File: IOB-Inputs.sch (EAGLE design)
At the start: 22 parts, among them J1 RJ12/6, Q0 P-FET, Q1 P-FET, Q2 P-FET, Q3 P-FET

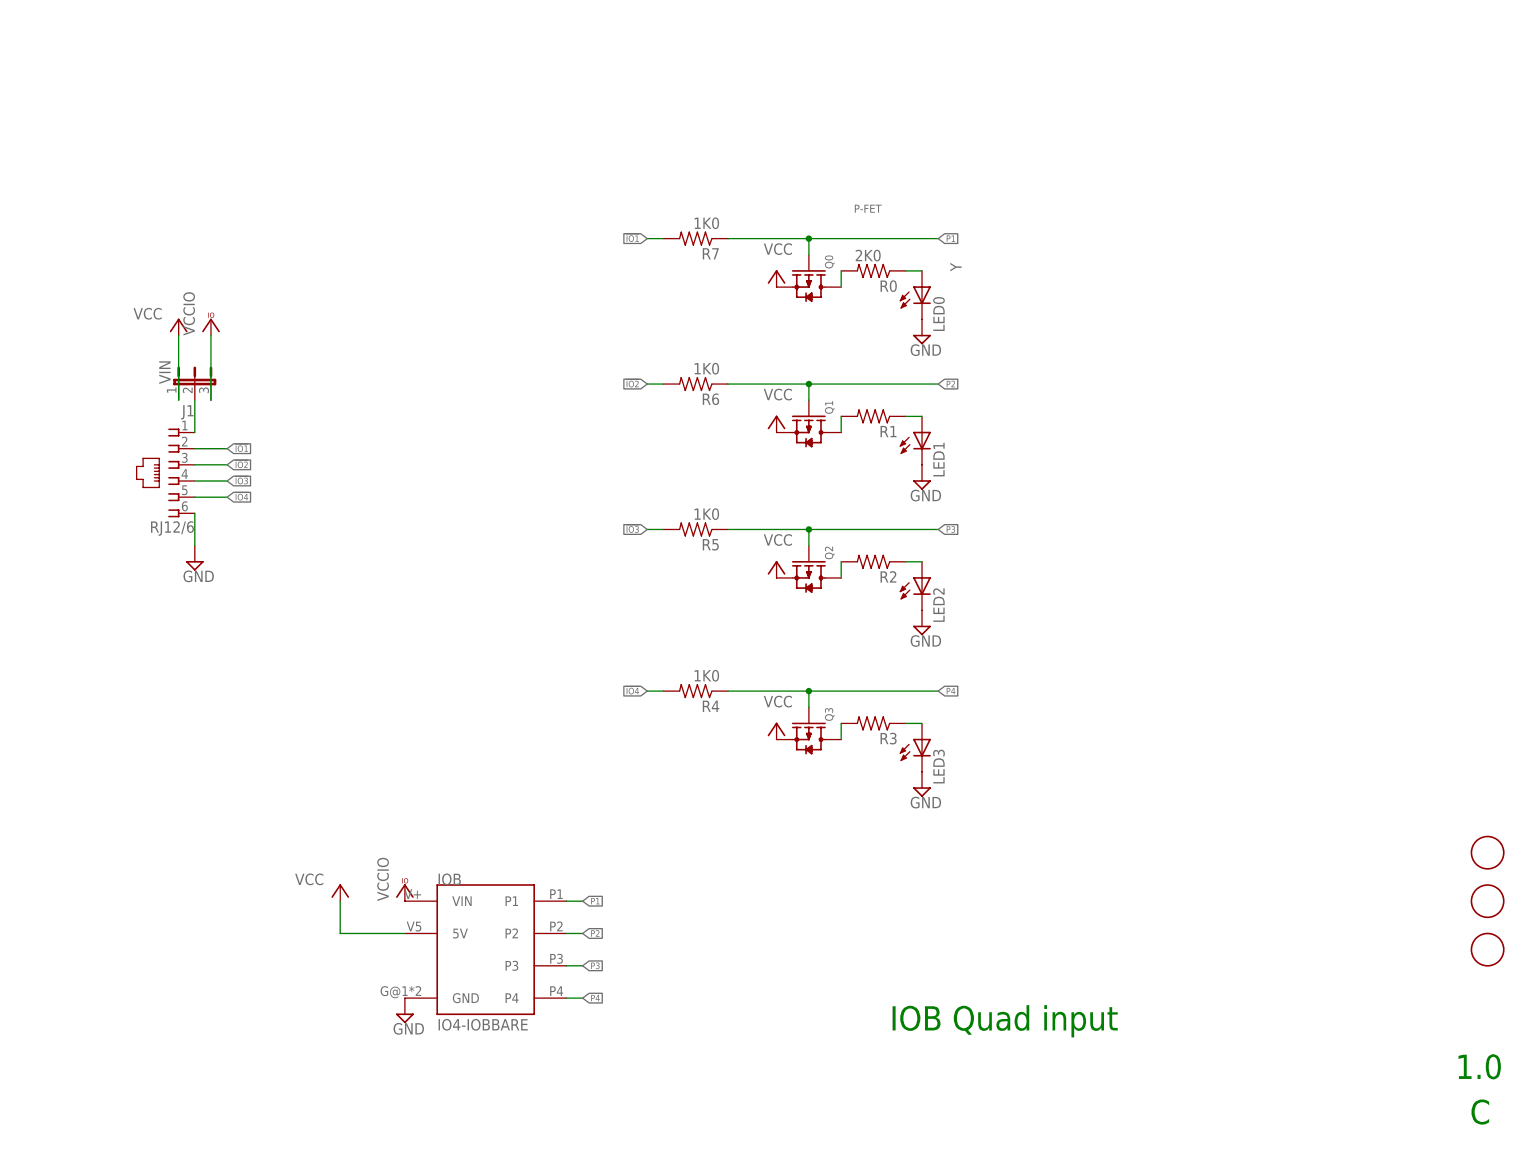
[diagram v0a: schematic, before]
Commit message: added input protection diodes and RC filter to handle 1khz or less signals
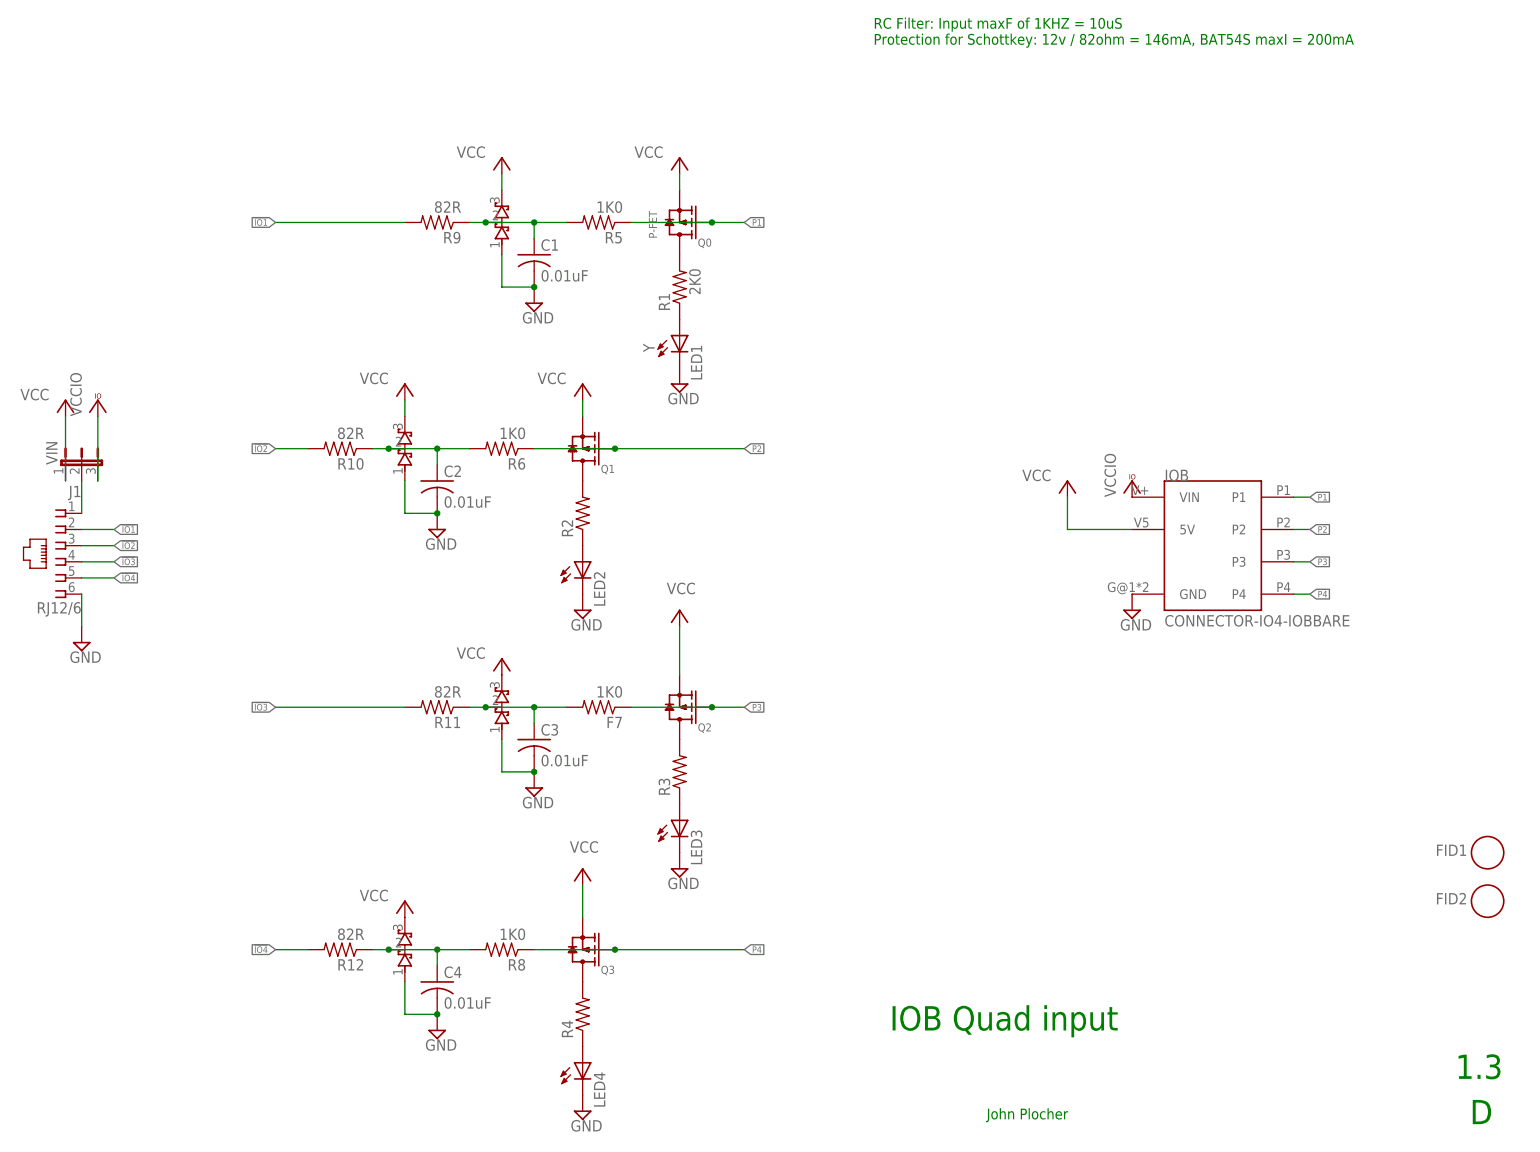
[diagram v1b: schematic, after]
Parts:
- removed FID3: FIDUCIAL, SPCoast:FIDUCIAL
- removed LED0: Y, SPCoast:LED0603-LED
- removed R0: 2K0, SPCoast:R0805-RES
- removed R7: 1K0, SPCoast:R0805-RES
- added C1, C2, C3, C4: 0.01uF, SPCoast:CAP0603
- added D1, D2, D3, D4: (no value), SPCoast:DIODE-BAT54S323R
- added F7, R8: 1K0, SPCoast:R0805-RES
- added LED4: Y, SPCoast:LED0603-LED
- added R10, R11, R12, R9: 82R, SPCoast:R0805-RES
- IOB: value IO4-IOBBARE -> CONNECTOR-IO4-IOBBARE; device SPCoast:IO4-IOBBARE -> SPCoast:CONNECTOR-IO4-IOBBARE
- J1: device SPCoast:CONNECTOR-RJ25CORCOM -> SPCoast:CONNECTOR-RJ25-6P6C
- R4: value 1K0 -> 2K0
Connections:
- removed net N$2 (its old number): LED0.A, R0.1
- new net N$10: C4.1, D4.COM, R12.1, R8.2
- new net N$12: C3.1, D3.COM, F7.2, R11.1
- new net N$13: C2.1, D2.COM, R10.1, R6.2
- new net N$14: C1.1, D1.COM, R5.2, R9.1
- new net N$5: LED4.A, R4.1
- net !IO1: now also R9.2; no longer R7.2
- net !IO2: now also R10.2; no longer R6.2
- net !IO3: now also R11.2; no longer R5.2
- net !IO4: now also R12.2; no longer R4.2
- net GND: now also C1.2, C2.2, C3.2, C4.2, D1.A1, D2.A1, D3.A1, D4.A1, LED4.C; no longer LED0.C
- net N$11: now also R1.2; no longer R0.2
- net N$30: now also R2.2; no longer R1.2
- net N$31: now also R3.2; no longer R2.2
- net N$32: now also R4.2; no longer R3.2
- net P1: now also R5.1; no longer R7.1
- net P3: now also F7.1; no longer R5.1
- net P4: now also R8.1; no longer R4.1
- net VCC: now also D1.C2, D2.C2, D3.C2, D4.C2
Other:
- note added: "1.3"
- note added: "D"
- note added: "John Plocher"
- note added: "RC Filter: Input maxF of 1KHZ = 10uS Protection for Schottkey: 12v / 82ohm = 146mA, BAT54S maxI = 200mA"
- note removed: "1.0"
- note removed: "C"
- moved on the sheet: IOB, J1, LED1, LED2, LED3, Q0, Q1, Q2, Q3, R1, R2, R3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

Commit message: added 6x1 0.100 header
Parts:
- added CON1: (no value), SPCoast:CONNECTOR-M06LOCK
- renumbered F7 to R7
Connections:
- net !IO1: now also CON1.2
- net !IO2: now also CON1.3
- net !IO3: now also CON1.4
- net !IO4: now also CON1.5
- net GND: now also CON1.6
- net N$1: now also CON1.1
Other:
- note added: "1.3 => 1.4: Added CON1, 6-pin 0.100"
- note added: "1.4"
- note removed: "1.3"
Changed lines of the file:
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@@
 <part name="Q3" library="SPCoast" deviceset="MOSFET-P" device="-044021001" value="P-FET"/>
 <part name="R8" library="SPCoast" deviceset="R*" device="0805-RES" value="1K0"/>
-<part name="F7" library="SPCoast" deviceset="R*" device="0805-RES" value="1K0"/>
+<part name="R7" library="SPCoast" deviceset="R*" device="0805-RES" value="1K0"/>
 <part name="R6" library="SPCoast" deviceset="R*" device="0805-RES" value="1K0"/>
 <part name="R5" library="SPCoast" deviceset="R*" device="0805-RES" value="1K0"/>
@@
 <part name="P+9" library="supply1" deviceset="VCC" device=""/>
 <part name="P+10" library="supply1" deviceset="VCC" device=""/>
+<part name="CON1" library="SPCoast" deviceset="CONNECTOR-M06" device="LOCK"/>
 </parts>
 <sheets>
@@
 <plain>
 <text x="149.86" y="20.32" size="3.81" layer="91">IOB Quad input</text>
-<text x="238.76" y="12.7" size="3.81" layer="91">1.3</text>
+<text x="238.76" y="12.7" size="3.81" layer="91">1.4</text>
 <text x="241.046" y="5.588" size="3.81" layer="91">D</text>
 <text x="147.32" y="175.26" size="1.6764" layer="91">RC Filter: Input maxF of 1KHZ = 10uS
 Protection for Schottkey: 12v / 82ohm = 146mA, BAT54S maxI = 200mA</text>
 <text x="165.1" y="6.35" size="1.6764" layer="91" ratio="14">John Plocher</text>
+<text x="149.86" y="30.48" size="1.6764" layer="91">1.3 =&gt; 1.4: Added CON1, 6-pin 0.100</text>
 </plain>
 <instances>
@@
 <attribute name="VALUE" x="92.71" y="36.322" size="1.778" layer="96" rot="R180"/>
 </instance>
-<instance part="F7" gate="R" x="104.14" y="71.12" smashed="yes" rot="R180">
+<instance part="R7" gate="R" x="104.14" y="71.12" smashed="yes" rot="R180">
 <attribute name="NAME" x="107.95" y="69.6214" size="1.778" layer="95" rot="R180"/>
 <attribute name="VALUE" x="107.95" y="74.422" size="1.778" layer="96" rot="R180"/>
@@
 <attribute name="VALUE" x="71.12" y="40.64" size="1.778" layer="96" rot="MR0"/>
 </instance>
+<instance part="CON1" gate="J" x="40.64" y="96.52" rot="R180"/>
 </instances>
 <busses>
@@
 <pinref part="V14" gate="GND" pin="GND"/>
 <wire x1="22.86" y1="83.82" x2="22.86" y2="88.9" width="0.1524" layer="91"/>
+<pinref part="CON1" gate="J" pin="6"/>
+<wire x1="22.86" y1="88.9" x2="35.56" y2="88.9" width="0.1524" layer="91"/>
+<junction x="22.86" y="88.9"/>
 </segment>
 <segment>
@@
 <label x="127" y="71.12" size="1.016" layer="95" xref="yes"/>
 <pinref part="Q2" gate="Q" pin="G"/>
-<pinref part="F7" gate="R" pin="1"/>
+<pinref part="R7" gate="R" pin="1"/>
 <wire x1="109.22" y1="71.12" x2="121.92" y2="71.12" width="0.1524" layer="91"/>
 <junction x="121.92" y="71.12"/>
@@
 <net name="!IO1" class="2">
 <segment>
-<wire x1="27.94" y1="99.06" x2="22.86" y2="99.06" width="0.1524" layer="91"/>
 <pinref part="J1" gate="J" pin="2"/>
-<label x="27.94" y="99.06" size="1.016" layer="95" xref="yes"/>
+<label x="45.72" y="99.06" size="1.016" layer="95" xref="yes"/>
+<pinref part="CON1" gate="J" pin="2"/>
+<wire x1="22.86" y1="99.06" x2="35.56" y2="99.06" width="0.1524" layer="91"/>
 </segment>
 <segment>
@@
 <net name="!IO2" class="2">
 <segment>
-<wire x1="27.94" y1="96.52" x2="22.86" y2="96.52" width="0.1524" layer="91"/>
 <pinref part="J1" gate="J" pin="3"/>
-<label x="27.94" y="96.52" size="1.016" layer="95" xref="yes"/>
+<label x="45.72" y="96.52" size="1.016" layer="95" xref="yes"/>
+<pinref part="CON1" gate="J" pin="3"/>
+<wire x1="22.86" y1="96.52" x2="35.56" y2="96.52" width="0.1524" layer="91"/>
 </segment>
 <segment>
@@
 <net name="!IO3" class="2">
 <segment>
-<wire x1="27.94" y1="93.98" x2="22.86" y2="93.98" width="0.1524" layer="91"/>
 <pinref part="J1" gate="J" pin="4"/>
-<label x="27.94" y="93.98" size="1.016" layer="95" xref="yes"/>
+<label x="45.72" y="93.98" size="1.016" layer="95" xref="yes"/>
+<pinref part="CON1" gate="J" pin="4"/>
+<wire x1="22.86" y1="93.98" x2="35.56" y2="93.98" width="0.1524" layer="91"/>
 </segment>
 <segment>
@@
 <net name="!IO4" class="2">
 <segment>
-<wire x1="27.94" y1="91.44" x2="22.86" y2="91.44" width="0.1524" layer="91"/>
 <pinref part="J1" gate="J" pin="5"/>
-<label x="27.94" y="91.44" size="1.016" layer="95" xref="yes"/>
+<label x="45.72" y="91.44" size="1.016" layer="95" xref="yes"/>
+<pinref part="CON1" gate="J" pin="5"/>
+<wire x1="22.86" y1="91.44" x2="35.56" y2="91.44" width="0.1524" layer="91"/>
 </segment>
 <segment>
@@
 <wire x1="22.86" y1="106.68" x2="22.86" y2="101.6" width="0.1524" layer="91"/>
 <pinref part="VIN" gate="J" pin="2"/>
+<pinref part="CON1" gate="J" pin="1"/>
+<wire x1="22.86" y1="101.6" x2="35.56" y2="101.6" width="0.1524" layer="91"/>
+<junction x="22.86" y="101.6"/>
 </segment>
 </net>
@@
 <pinref part="D3" gate="G$1" pin="COM"/>
 <wire x1="83.82" y1="71.12" x2="86.36" y2="71.12" width="0.1524" layer="91"/>
-<pinref part="F7" gate="R" pin="2"/>
+<pinref part="R7" gate="R" pin="2"/>
 <wire x1="86.36" y1="71.12" x2="93.98" y2="71.12" width="0.1524" layer="91"/>
 <junction x="86.36" y="71.12"/>

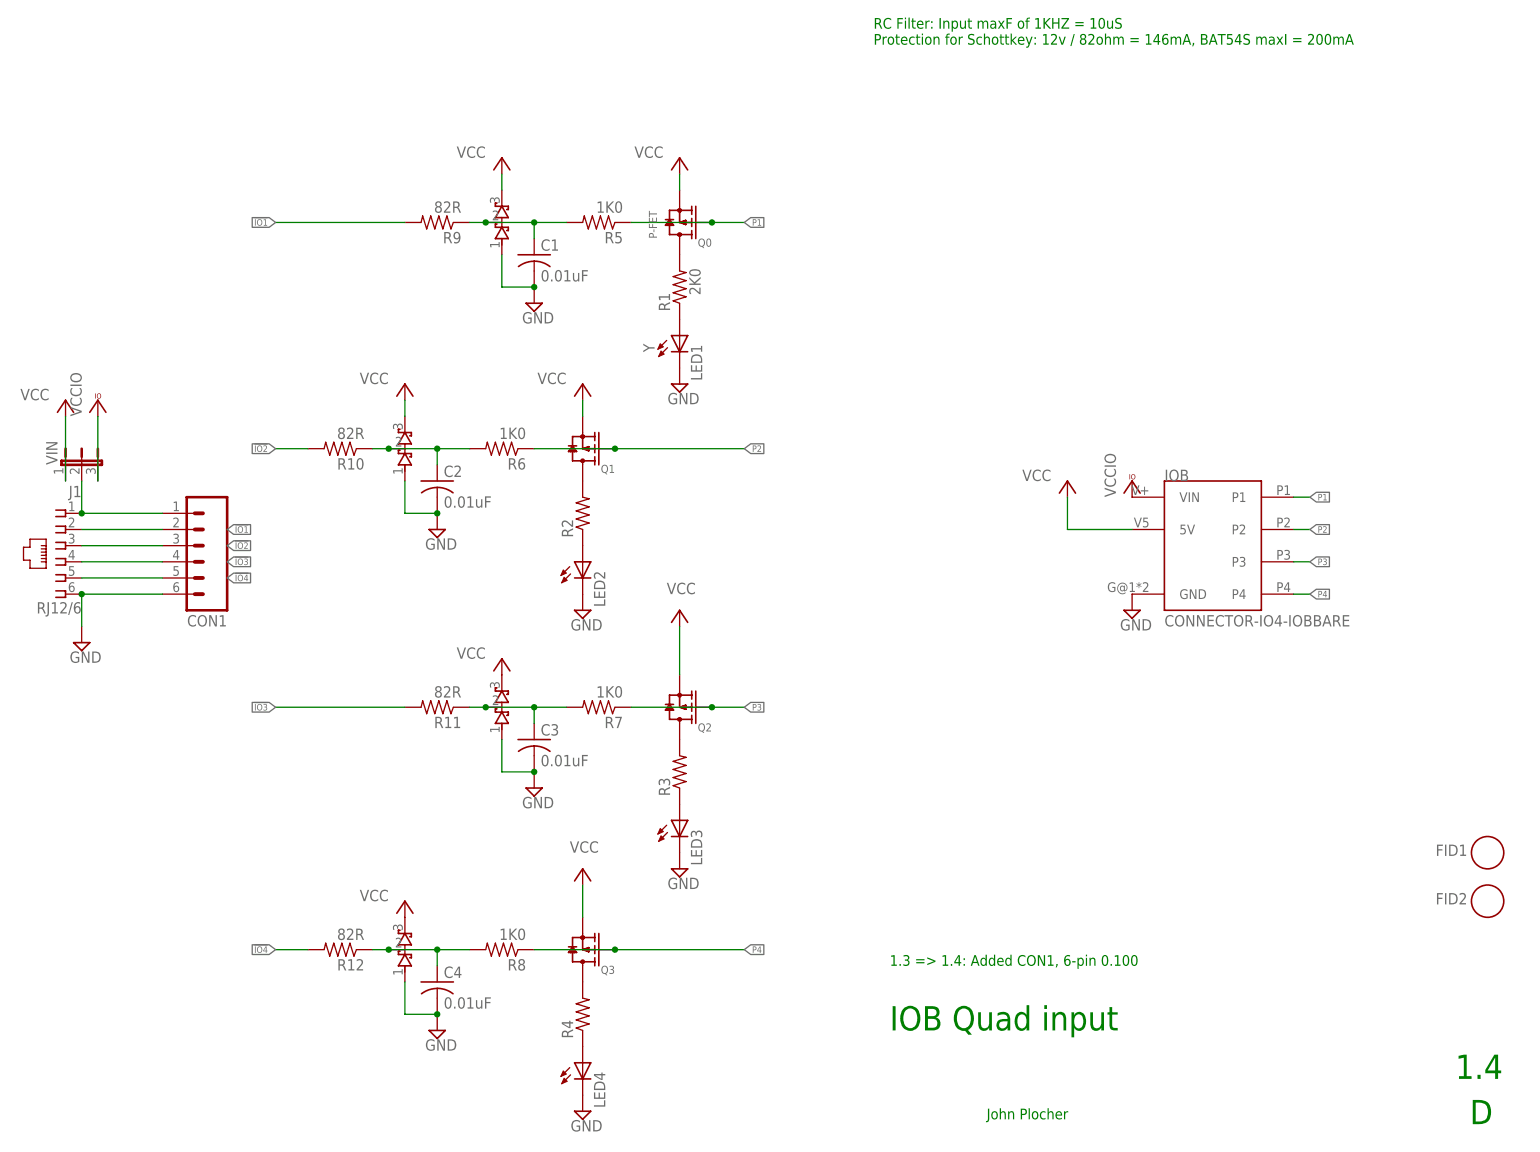
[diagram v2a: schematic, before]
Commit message: new IOB design
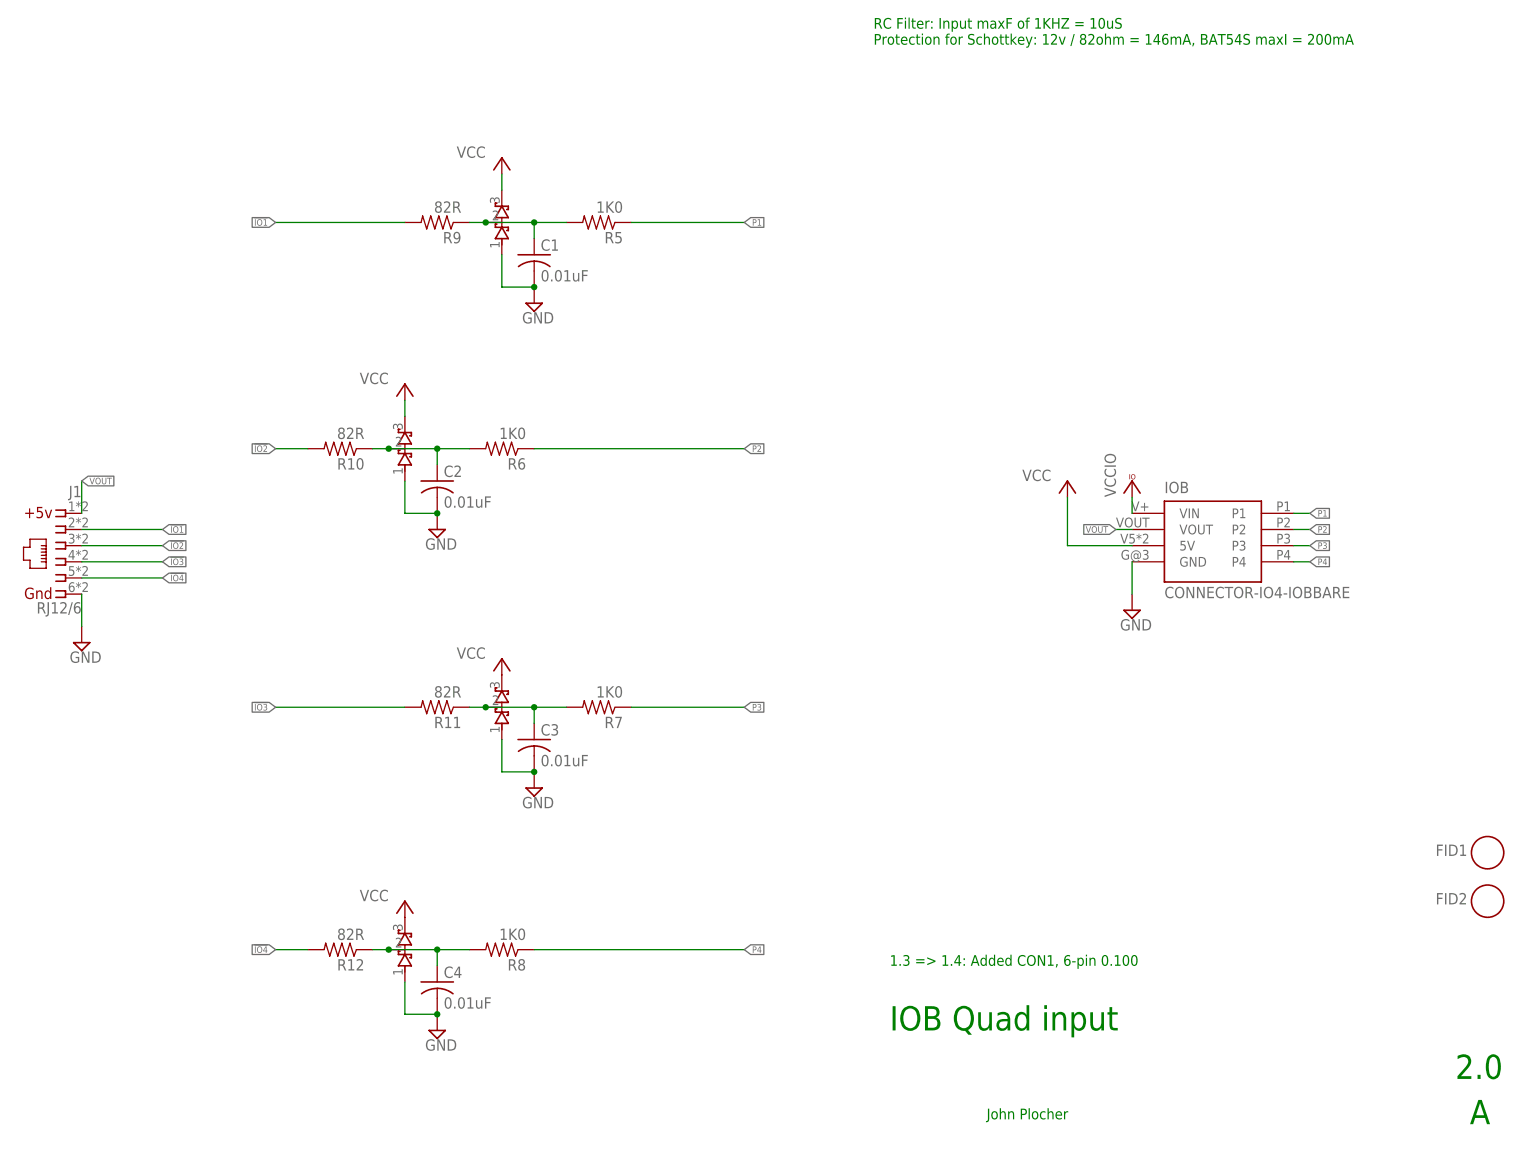
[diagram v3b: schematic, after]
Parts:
- removed CON1: (no value), SPCoast:CONNECTOR-M06LOCK
- removed LED1, LED2, LED3, LED4: Y, SPCoast:LED0603-LED
- removed Q0, Q1, Q2, Q3: P-FET, SPCoast:MOSFET-P-044021001
- removed R1, R2, R3, R4: 2K0, SPCoast:R0805-RES
- removed VIN: (no value), SPCoast:JUMPER-3PTH-LOCK
- J1: device SPCoast:CONNECTOR-RJ25-6P6C -> SPCoast:CONNECTOR-IO4IPINS
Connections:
- removed net N$1: CON1.1, J1.1, VIN.2
- removed net N$11: Q0.D, R1.2
- removed net N$2: LED1.A, R1.1
- removed net N$3: LED2.A, R2.1
- removed net N$30: Q1.D, R2.2
- removed net N$31: Q2.D, R3.2
- removed net N$32: Q3.D, R4.2
- removed net N$4: LED3.A, R3.1
- removed net N$5: LED4.A, R4.1
- new net VOUT: IOB.VOUT, J1.1
- net !IO1: no longer CON1.2
- net !IO2: no longer CON1.3
- net !IO3: no longer CON1.4
- net !IO4: no longer CON1.5
- net GND: no longer CON1.6, LED1.C, LED2.C, LED3.C, LED4.C
- net P1: no longer Q0.G
- net P2: no longer Q1.G
- net P3: no longer Q2.G
- net P4: no longer Q3.G
- net VCC: no longer Q0.S, Q1.S, Q2.S, Q3.S, VIN.1
- net VCCIO: no longer VIN.3
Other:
- note added: "2.0"
- note added: "A"
- note removed: "1.4"
- note removed: "D"
